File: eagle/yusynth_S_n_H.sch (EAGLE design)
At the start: 35 parts, among them IC1 TL074P, Q1 BF245, T1 2N3904

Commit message: almost routed
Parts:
- added C11: 10u, rcl:CPOL-USB45181A
- added D1: 1N4148DO35-7, diode:1N4148DO35-7
- added IC2: TL071P, linear:TL071P
- added INT_EXT: 9077-1, switch-misc:9077-1
- added R12: 2k2, rcl:R-US_0207/10
- added R13: 100k, rcl:R-US_0207/10
- added R14: 120k, rcl:R-US_0207/10
- added RATE: 500k rev log, pot:3RP/1610N
- D4: value 1N4148DO35-7 -> 1N4148DO35-10; device diode:1N4148DO35-7 -> diode:1N4148DO35-10
- renumbered IN to SIGNAL_IN
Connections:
- new net N$22: IC2.+IN, R13.2, R14.2
- new net N$23: C11.+, IC2.-IN, R12.1
- new net N$24: R12.2, RATE.A
- new net N$25: D1.A, IC2.OUT, R14.1, RATE.S
- new net N$26: D1.C, INT_EXT.P
- net +12V: now also IC2.V+
- net -12V: now also C11.-, IC2.V-
- net GND: now also R13.1
- net N$3: now also INT_EXT.S
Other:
- moved on the sheet: C1, C2, C4, C5, C6, C8, PWR1, SLEW, U$1, U$2

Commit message: fixed an opamp output connection and spacing tweaks
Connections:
- net N$11: now also IC1D.OUT
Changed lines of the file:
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@@
 <?xml version="1.0" encoding="utf-8"?>
 <!DOCTYPE eagle SYSTEM "eagle.dtd">
-<eagle version="7.2.0">
+<eagle version="7.1.0">
 <drawing>
 <settings>
@@
 <wire x1="139.7" y1="114.3" x2="154.94" y2="114.3" width="0.1524" layer="91"/>
 <junction x="154.94" y="114.3"/>
-</segment>
-</net>
+<pinref part="IC1" gate="D" pin="OUT"/>
+</segment>
+</net>

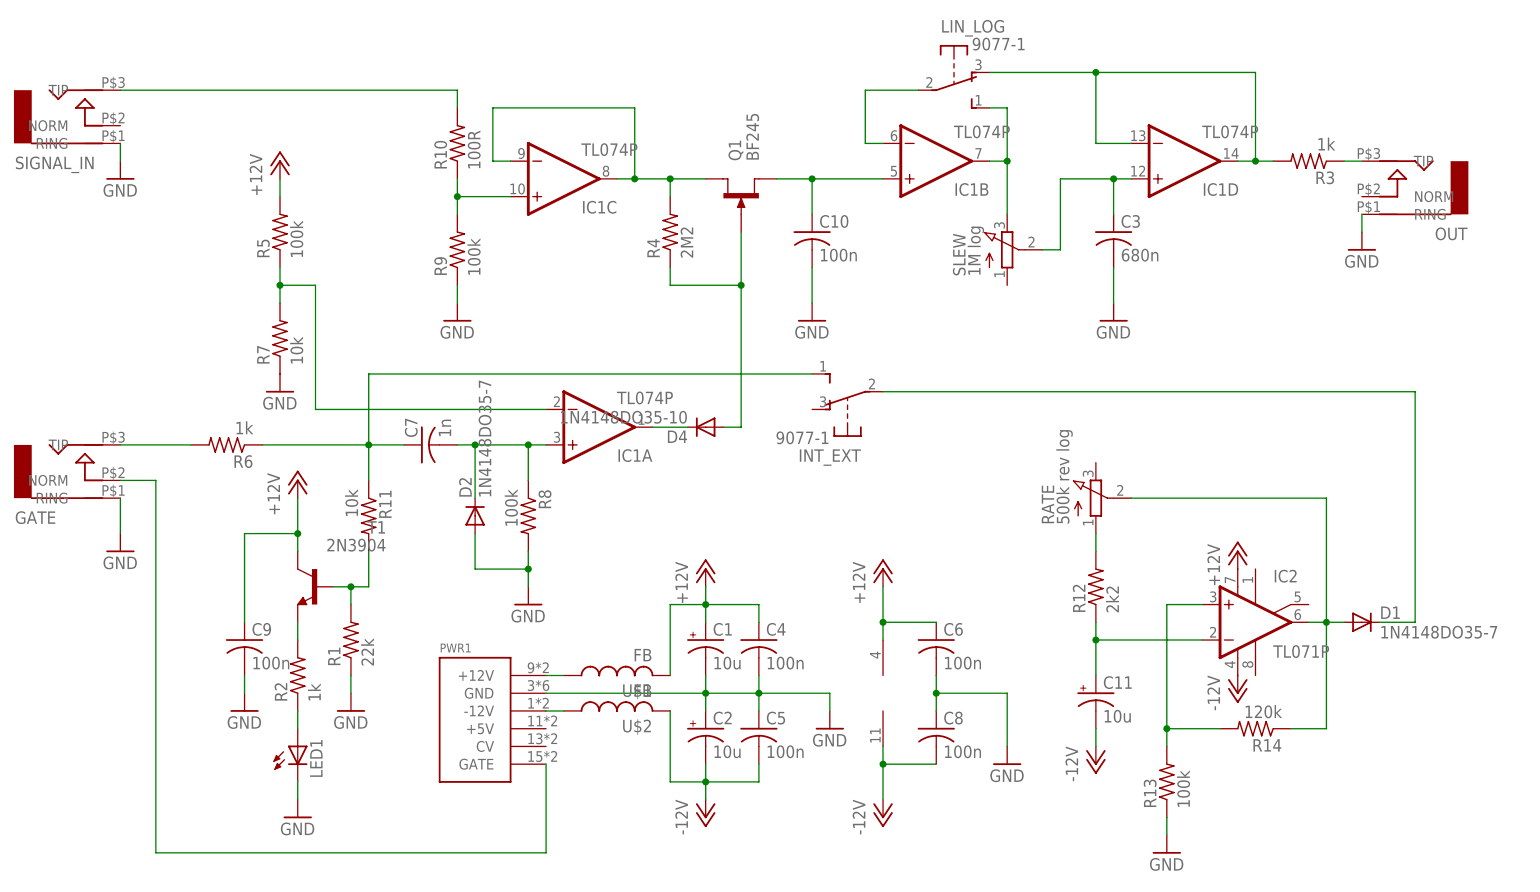
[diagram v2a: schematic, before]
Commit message: adjusted a spacing, removed ridiculous bus gate and corrected pot reversals
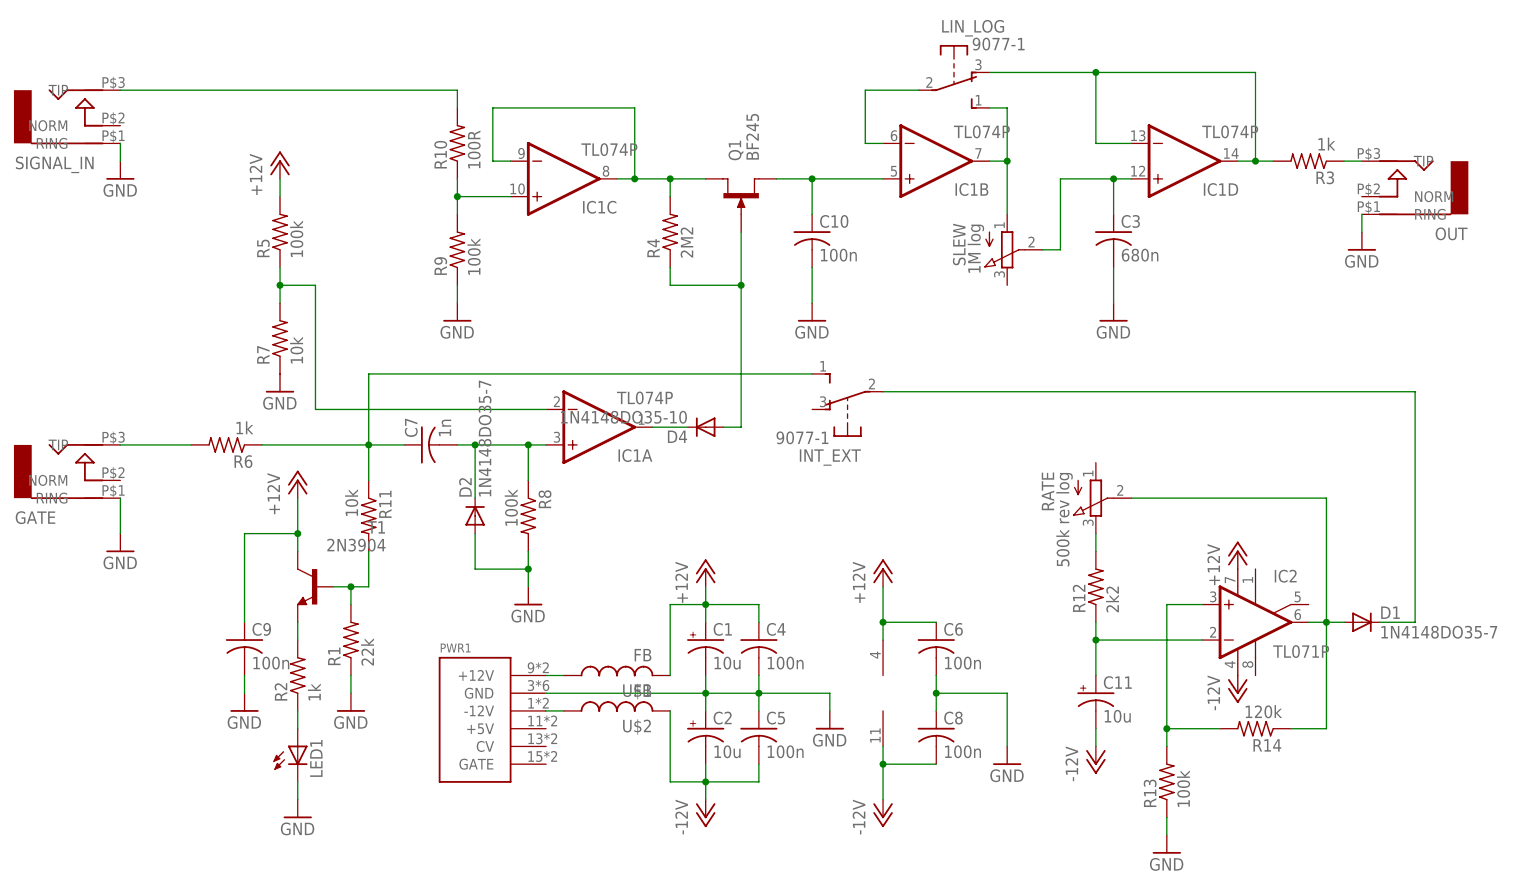
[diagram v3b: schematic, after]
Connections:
- removed net N$24: R12.2, RATE.A
- net N$12: now also R12.2, RATE.E; no longer GATE.NORM, PWR1.GATE
- net N$19: now also SLEW.A; no longer SLEW.E
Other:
- moved on the sheet: RATE, SLEW
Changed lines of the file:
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@@
 <instance part="R7" gate="G$1" x="38.1" y="76.2" rot="R90"/>
 <instance part="R8" gate="G$1" x="73.66" y="50.8" rot="R270"/>
-<instance part="SLEW" gate="G$1" x="142.24" y="88.9"/>
+<instance part="SLEW" gate="G$1" x="142.24" y="88.9" rot="MR180"/>
 <instance part="C4" gate="G$1" x="106.68" y="33.02"/>
 <instance part="C5" gate="G$1" x="106.68" y="20.32"/>
@@
 <instance part="R12" gate="G$1" x="154.94" y="40.64" rot="R90"/>
 <instance part="R13" gate="G$1" x="165.1" y="12.7" rot="R90"/>
-<instance part="RATE" gate="G$1" x="154.94" y="53.34"/>
+<instance part="RATE" gate="G$1" x="154.94" y="53.34" rot="MR180"/>
 <instance part="C11" gate="G$1" x="154.94" y="25.4"/>
 <instance part="P-3" gate="1" x="154.94" y="15.24"/>
@@
 </segment>
 </net>
-<net name="N$12" class="0">
-<segment>
-<pinref part="GATE" gate="G$1" pin="NORM"/>
-<wire x1="20.32" y1="55.88" x2="15.24" y2="55.88" width="0.1524" layer="91"/>
-<pinref part="PWR1" gate="G$1" pin="GATE"/>
-<wire x1="76.2" y1="15.24" x2="76.2" y2="2.54" width="0.1524" layer="91"/>
-<wire x1="76.2" y1="2.54" x2="20.32" y2="2.54" width="0.1524" layer="91"/>
-<wire x1="20.32" y1="2.54" x2="20.32" y2="55.88" width="0.1524" layer="91"/>
-</segment>
-</net>
 <net name="N$14" class="0">
 <segment>
@@
 <wire x1="157.48" y1="99.06" x2="149.86" y2="99.06" width="0.1524" layer="91"/>
 <wire x1="149.86" y1="99.06" x2="149.86" y2="88.9" width="0.1524" layer="91"/>
-<pinref part="SLEW" gate="G$1" pin="S"/>
-<wire x1="149.86" y1="88.9" x2="147.32" y2="88.9" width="0.1524" layer="91"/>
 <pinref part="C3" gate="G$1" pin="1"/>
 <wire x1="157.48" y1="93.98" x2="157.48" y2="99.06" width="0.1524" layer="91"/>
 <junction x="157.48" y="99.06"/>
+<pinref part="SLEW" gate="G$1" pin="S"/>
+<wire x1="147.32" y1="88.9" x2="149.86" y2="88.9" width="0.1524" layer="91"/>
 </segment>
 </net>
 <net name="N$19" class="0">
 <segment>
-<pinref part="SLEW" gate="G$1" pin="E"/>
 <pinref part="IC1" gate="B" pin="OUT"/>
-<wire x1="142.24" y1="93.98" x2="142.24" y2="101.6" width="0.1524" layer="91"/>
 <wire x1="142.24" y1="101.6" x2="139.7" y2="101.6" width="0.1524" layer="91"/>
 <wire x1="142.24" y1="101.6" x2="142.24" y2="109.22" width="0.1524" layer="91"/>
-<junction x="142.24" y="101.6"/>
 <pinref part="LIN_LOG" gate="1" pin="S"/>
 <wire x1="142.24" y1="109.22" x2="139.7" y2="109.22" width="0.1524" layer="91"/>
+<pinref part="SLEW" gate="G$1" pin="A"/>
+<wire x1="142.24" y1="93.98" x2="142.24" y2="101.6" width="0.1524" layer="91"/>
+<junction x="142.24" y="101.6"/>
 </segment>
 </net>
@@
 </segment>
 </net>
-<net name="N$24" class="0">
-<segment>
-<pinref part="R12" gate="G$1" pin="2"/>
-<pinref part="RATE" gate="G$1" pin="A"/>
-<wire x1="154.94" y1="45.72" x2="154.94" y2="48.26" width="0.1524" layer="91"/>
-</segment>
-</net>
 <net name="N$25" class="0">
 <segment>
@@
 <wire x1="187.96" y1="35.56" x2="187.96" y2="53.34" width="0.1524" layer="91"/>
 <junction x="187.96" y="35.56"/>
-<pinref part="RATE" gate="G$1" pin="S"/>
-<wire x1="160.02" y1="53.34" x2="187.96" y2="53.34" width="0.1524" layer="91"/>
 <pinref part="R14" gate="G$1" pin="1"/>
 <wire x1="182.88" y1="20.32" x2="187.96" y2="20.32" width="0.1524" layer="91"/>
 <wire x1="187.96" y1="20.32" x2="187.96" y2="35.56" width="0.1524" layer="91"/>
+<pinref part="RATE" gate="G$1" pin="S"/>
+<wire x1="160.02" y1="53.34" x2="187.96" y2="53.34" width="0.1524" layer="91"/>
 </segment>
 </net>
@@
 </segment>
 </net>
+<net name="N$12" class="0">
+<segment>
+<pinref part="RATE" gate="G$1" pin="E"/>
+<pinref part="R12" gate="G$1" pin="2"/>
+<wire x1="154.94" y1="48.26" x2="154.94" y2="45.72" width="0.1524" layer="91"/>
+</segment>
+</net>
